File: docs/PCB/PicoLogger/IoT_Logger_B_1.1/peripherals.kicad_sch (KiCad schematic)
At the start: 71 parts, among them Q3 BC817-40-DIO, Q4 BSS138, SW3 Tact Switch 6x6mm / 13mm, SW4 Tact Switch 6x6mm / 13mm, U4 PCA9306DCUR, U5 SN65HVD230DR, U6 MCP7940N-xSN, U8 FM24CL16B, U9 MX25L25673GM2I-08G, Y3 QT3CD-32.768KEZY-T

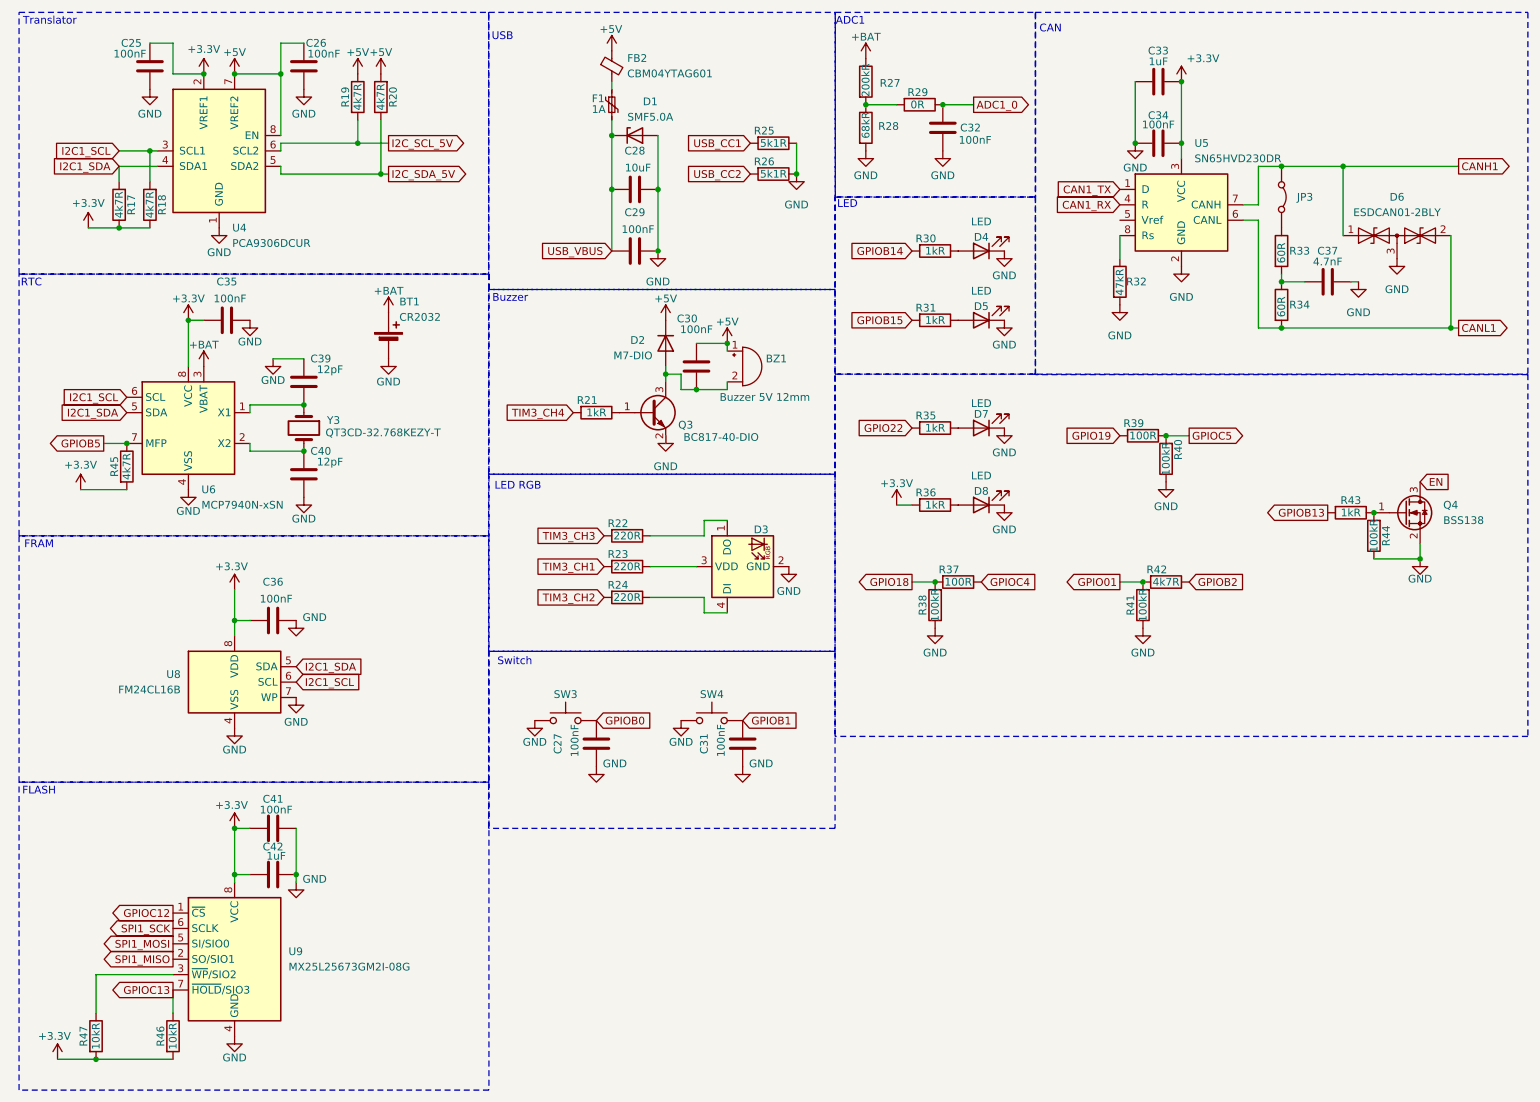
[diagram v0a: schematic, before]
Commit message: New logger revisions added.
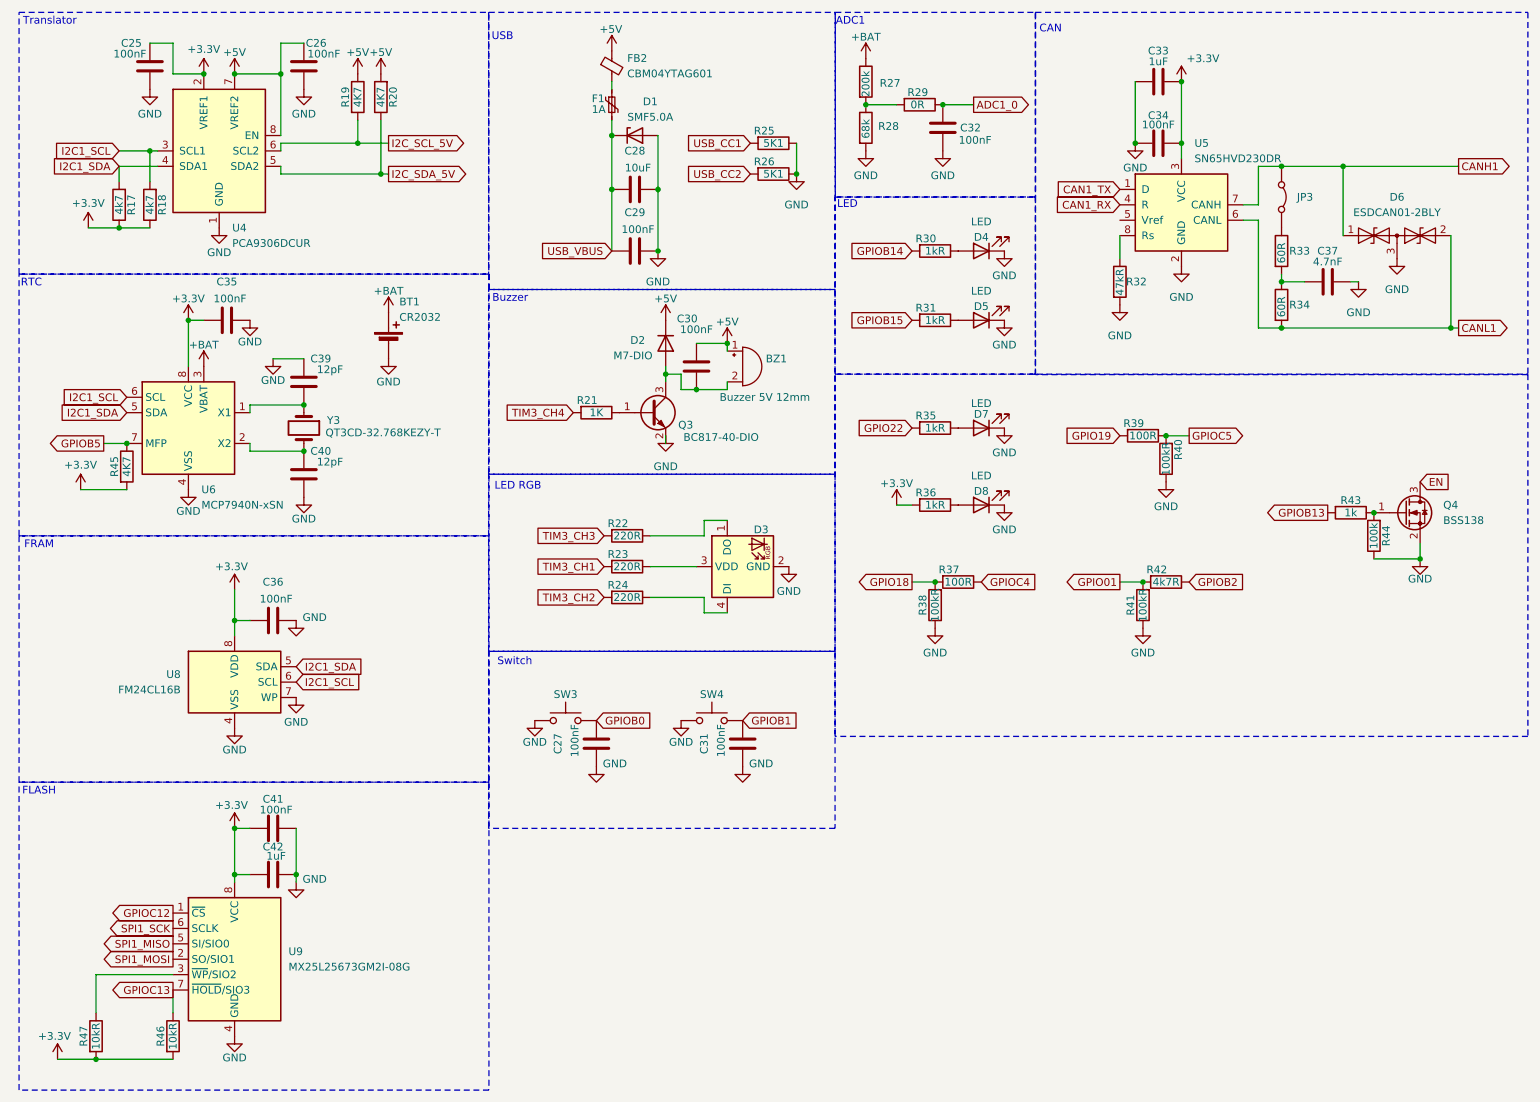
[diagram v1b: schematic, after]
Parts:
- R17, R18: value 4k7R -> 4k7
- R19, R20, R45: value 4k7R -> 4K7
- R21: value 1kR -> 1K
- R25, R26: value 5k1R -> 5K1
- R27: value 200kR -> 200k
- R28: value 68kR -> 68k
- R43: value 1kR -> 1k
- R44: value 100kR -> 100k
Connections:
- net SPI1_MISO: now also U9.5 (SI/SIO0); no longer U9.2 (SO/SIO1)
- net SPI1_MOSI: now also U9.2 (SO/SIO1); no longer U9.5 (SI/SIO0)
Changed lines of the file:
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@@
 		)
 	)
-	(global_label "SPI1_MISO"
+	(global_label "SPI1_MOSI"
 		(shape output)
 		(at 38.1 168.91 180)
@@
 		)
 	)
-	(global_label "SPI1_MOSI"
+	(global_label "SPI1_MISO"
 		(shape output)
 		(at 38.1 166.37 180)
@@
 			)
 		)
-		(property "Value" "4k7R"
+		(property "Value" "4k7"
 			(at 29.21 44.45 90)
 			(effects
@@
 			)
 		)
-		(property "Value" "4k7R"
+		(property "Value" "4K7"
 			(at 68.58 26.67 90)
 			(effects
@@
 			)
 		)
-		(property "Value" "5k1R"
+		(property "Value" "5K1"
 			(at 137.16 39.37 90)
 			(effects
@@
 			)
 		)
-		(property "Value" "4k7R"
+		(property "Value" "4k7"
 			(at 34.29 44.45 90)
 			(effects
@@
 			)
 		)
-		(property "Value" "4k7R"
+		(property "Value" "4K7"
 			(at 72.39 26.67 90)
 			(effects
@@
 			)
 		)
-		(property "Value" "4k7R"
+		(property "Value" "4K7"
 			(at 30.48 87.63 90)
 			(effects
@@
 			)
 		)
-		(property "Value" "100kR"
+		(property "Value" "100k"
 			(at 236.22 99.06 90)
 			(effects
@@
 			)
 		)
-		(property "Value" "5k1R"
+		(property "Value" "5K1"
 			(at 137.16 34.29 90)
 			(effects
@@
 			)
 		)
-		(property "Value" "200kR"
+		(property "Value" "200k"
 			(at 152.4 26.67 90)
 			(effects
@@
 			)
 		)
-		(property "Value" "1kR"
+		(property "Value" "1K"
 			(at 107.95 78.74 90)
 			(effects
@@
 			)
 		)
-		(property "Value" "1kR"
+		(property "Value" "1k"
 			(at 232.41 95.25 90)
 			(effects
@@
 			)
 		)
-		(property "Value" "68kR"
+		(property "Value" "68k"
 			(at 152.4 33.528 90)
 			(effects
